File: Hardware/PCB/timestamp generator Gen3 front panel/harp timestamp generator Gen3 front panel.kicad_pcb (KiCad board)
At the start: 2 copper layers, 133 x 35 mm, 13 parts

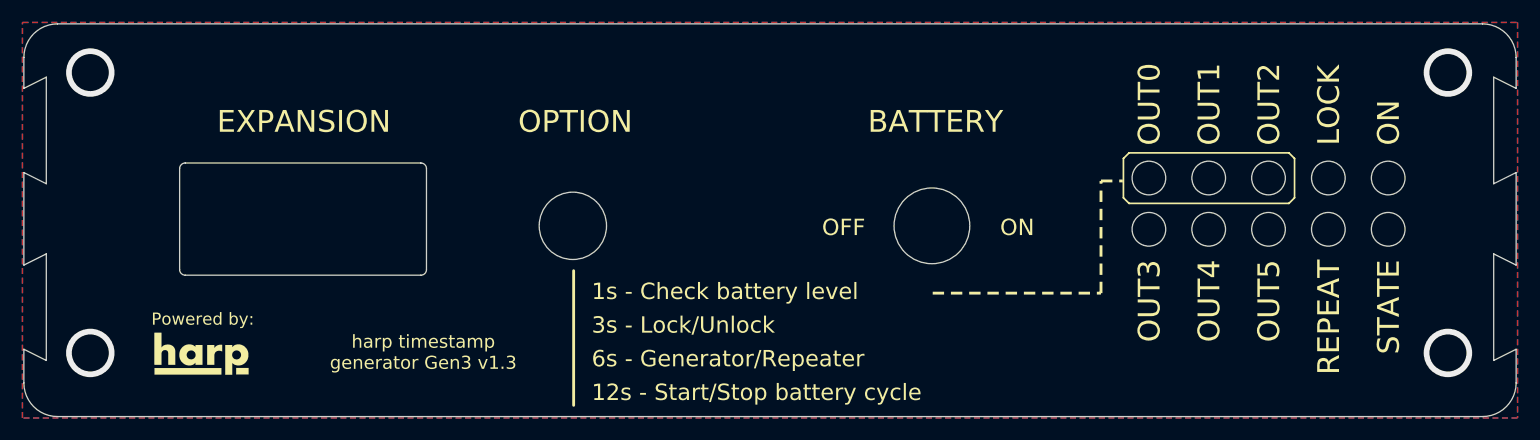
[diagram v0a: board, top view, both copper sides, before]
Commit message: Fix EXPANSION and BATTERY cuts in the front panel
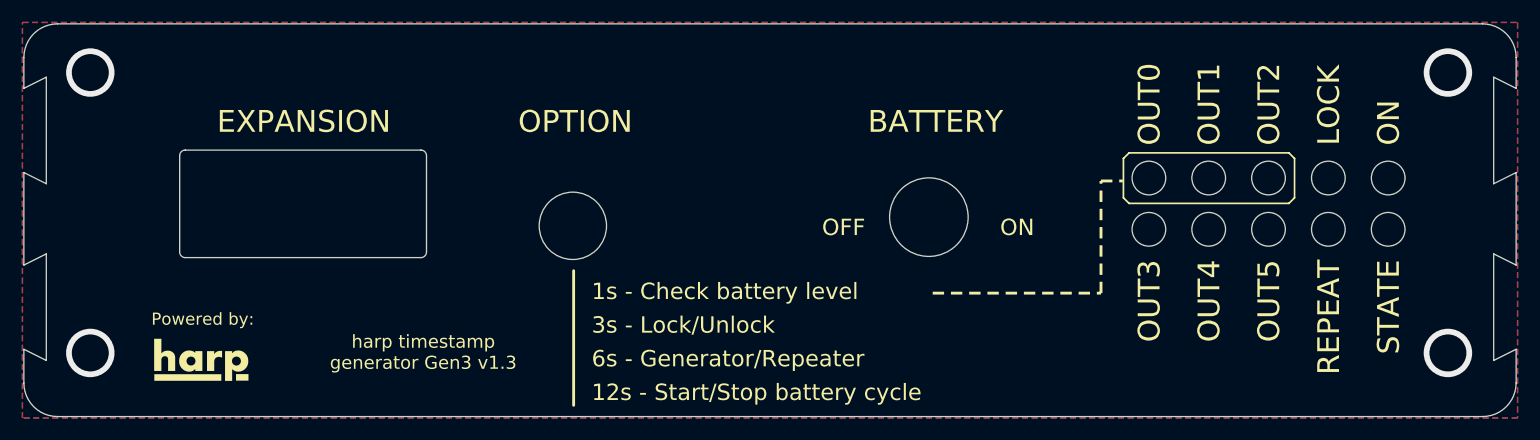
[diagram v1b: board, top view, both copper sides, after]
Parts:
- removed ref1: harp_logo, stepperdriver front panel:harp_logo
- added REF**: Fiducial_Cross_1.5mm_Mask2mm, Fiducial:Fiducial_Cross_1.5mm_Mask2mm, F.Cu at (144.2, 109.1)
- moved UNK_HOLE_11 0.82 mm to (162.7, 104.7)
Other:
- outline, holes or cut-outs redrawn
- board text added: "Powered by:"
